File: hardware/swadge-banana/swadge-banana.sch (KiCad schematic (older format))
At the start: 46 parts, among them J1 USB_B_Micro, SW1 SW_SPDT, U1 ESP-13-WROOM-02D, U2 OLED_DISPLAY, U3 BUS_PCIexpress, U4 QMA6981, U5 AP1117-33, U6 OLED_CONNECTOR

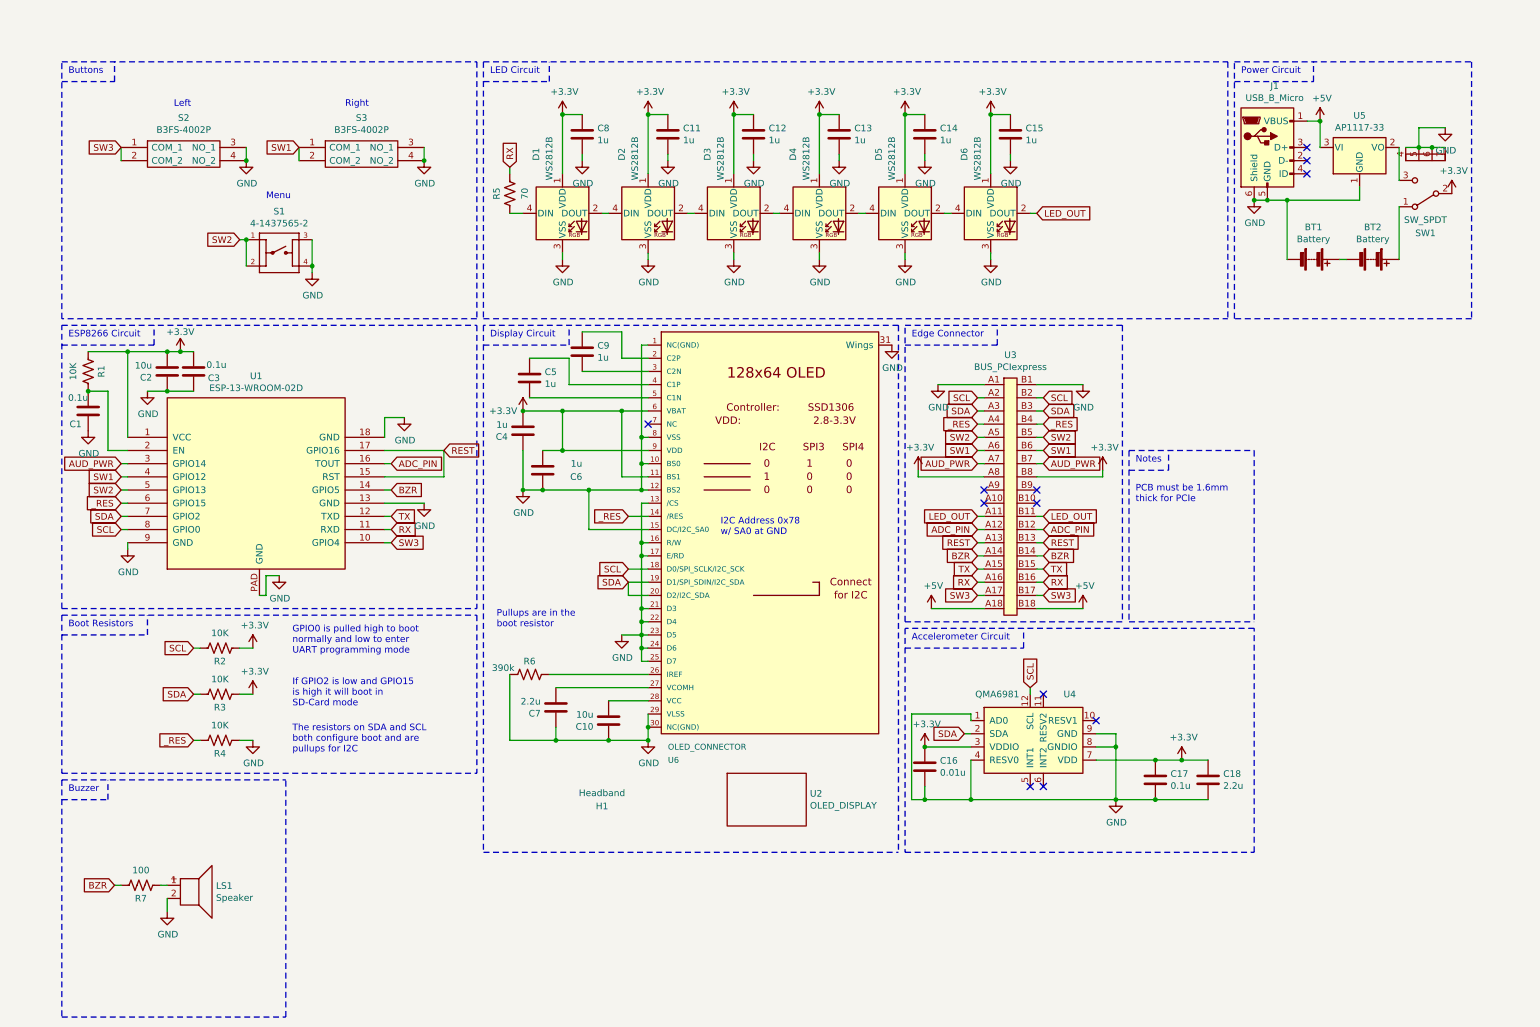
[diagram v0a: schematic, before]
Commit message: Updated banana sch/pcb from barrel
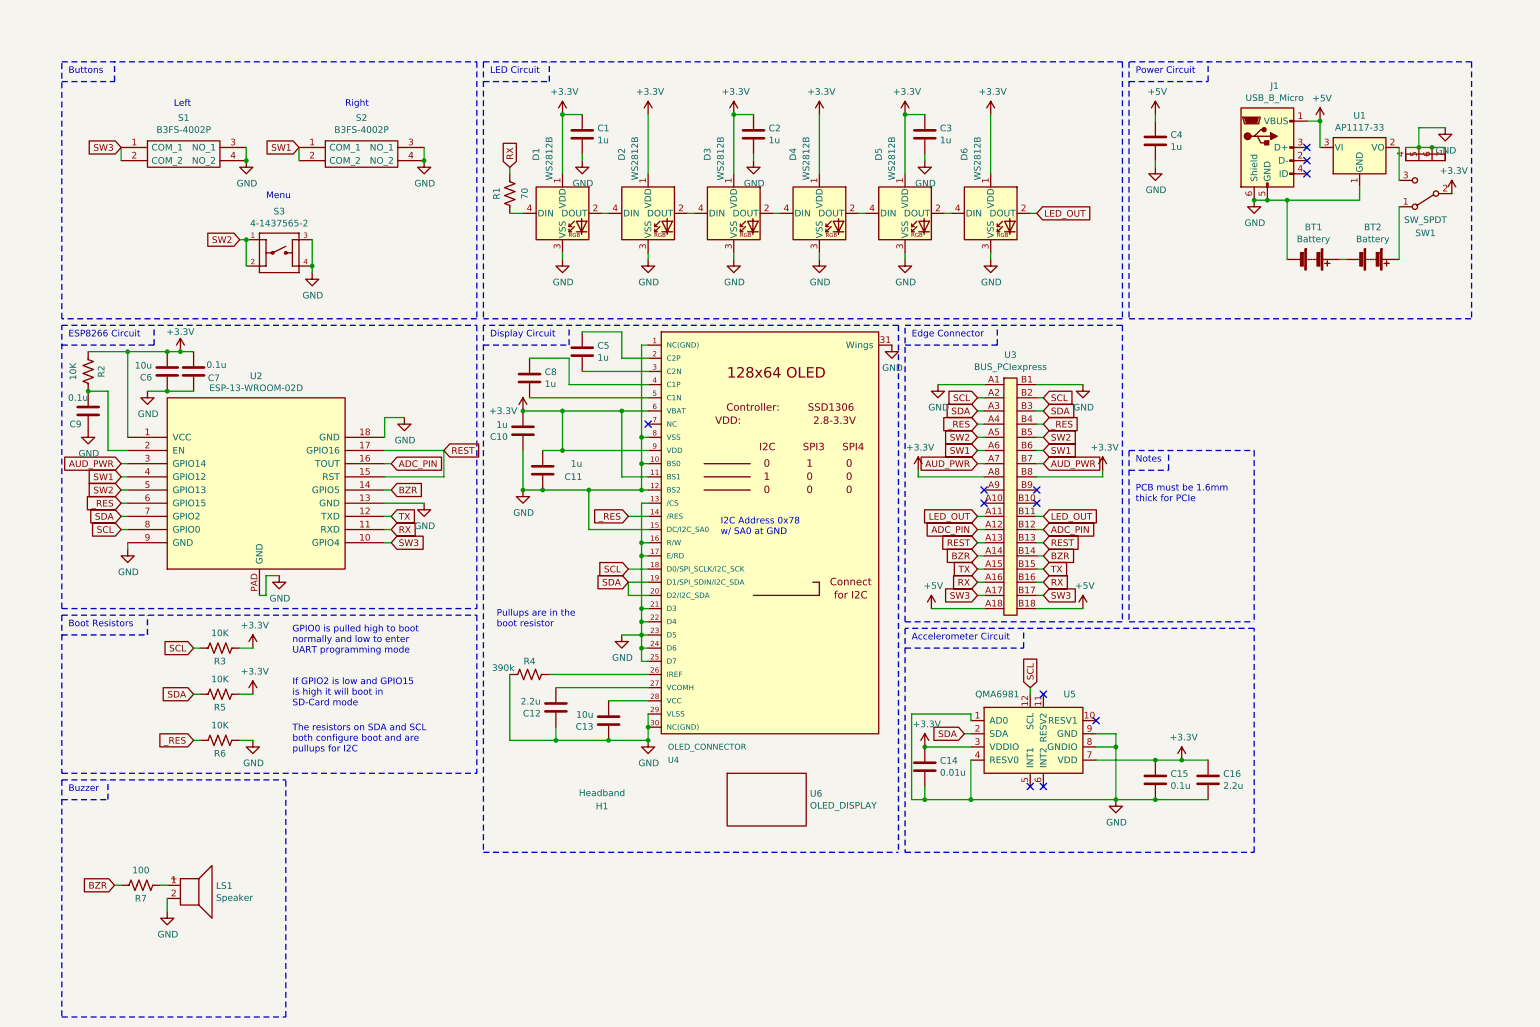
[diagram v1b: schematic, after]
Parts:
- removed C13, C15: 1u, Swadge_Parts:C_0603_1608Metric, symbol Swadge_Parts:C
- U4: renamed from U6; Digikey LCSC #C11095 -> LCSC Part #C11060; Notes Must have top contacts. same as the OLED -> Must have bottom contacts. same as the OLED
- U6: renamed from U2; Digikey EastRising# ER-OLED0.96-1.3W -> EastRising# ER-OLED0.96-1.1W; Notes Must be a single color. white. Must have SSD1306 driver. Mu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 -> Must be a single color; white. Must have SSD1306 driver. Mu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
- renumbered C8 to C1, C4 to C10, C6 to C11, C7 to C12, C10 to C13, C16 to C14, C17 to C15, C18 to C16, C12 to C2, C14 to C3, C11 to C4, C9 to C5, C2 to C6, C3 to C7, C5 to C8, C1 to C9, R5 to R1, R1 to R2, R2 to R3, R6 to R4, R3 to R5, R4 to R6, S2 to S1, S3 to S2, S1 to S3, U5 to U1, U1 to U2, U4 to U5
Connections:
- net +3V3: no longer C4.1
- net +5V: now also C4.1
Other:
- moved on the sheet: C4

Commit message: Merged cnlohr's changes
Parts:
- removed C4: 1u, Swadge_Parts:C_0603_1608Metric, symbol Swadge_Parts:C
- U2: renamed from U6; Digikey EastRising# ER-OLED0.96-1.1W -> EastRising# ER-OLED0.96-1.3W; Notes Must be a single color; white. Must have SSD1306 driver. Mu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 -> Must be a single color. white. Must have SSD1306 driver. Mu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
- U6: renamed from U4; Digikey LCSC Part #C11060 -> LCSC #C11095; Notes Must have bottom contacts. same as the OLED -> Must have top contacts. same as the OLED
- renumbered C9 to C1, C13 to C10, C2 to C12, C3 to C14, C14 to C16, C15 to C17, C16 to C18, C6 to C2, C7 to C3, C10 to C4, C8 to C5, C11 to C6, C12 to C7, C1 to C8, C5 to C9, R2 to R1, R3 to R2, R5 to R3, R6 to R4, R1 to R5, R4 to R6, S3 to S1, S1 to S2, S2 to S3, U2 to U1, U5 to U4, U1 to U5
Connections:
- net +3V3: no longer C3.2
- net +5V: now also C3.2
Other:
- moved on the sheet: C3

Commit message: Added power parts to Swadge_Parts library Modified swadge-banana.sch to use new power parts Removed cnlohr specific paths from sym-lib-table
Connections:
- net labels added: +3V3, +5V
- net labels removed: +3.3V-power, +5V-power
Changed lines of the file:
@@
 	1300 2700 1400 2700
 $Comp
-L 5050RGB:GND #PWR0102
+L Swadge_Parts:GND #PWR0102
 U 1 1 5DB48D54
 P 1900 1250
@@
 Connection ~ 1900 1250
 $Comp
-L 5050RGB:GND #PWR0103
+L Swadge_Parts:GND #PWR0103
 U 1 1 5DB4934E
 P 3250 1250
@@
 Connection ~ 3250 1250
 $Comp
-L 5050RGB:GND #PWR0104
+L Swadge_Parts:GND #PWR0104
 U 1 1 5DB4A3EF
 P 2400 2100
@@
 $EndComp
 $Comp
-L 5050RGB:GND #PWR0105
+L Swadge_Parts:GND #PWR0105
 U 1 1 5DB4B924
 P 3100 3200
@@
 $EndComp
 $Comp
-L 5050RGB:GND #PWR0101
+L Swadge_Parts:GND #PWR0101
 U 1 1 5DB4CC48
 P 1150 3000
@@
 $EndComp
 $Comp
-L 5050RGB:GND #PWR0106
+L Swadge_Parts:GND #PWR0106
 U 1 1 5DB4D3B3
 P 700 3300
@@
 $EndComp
 $Comp
-L 5050RGB:GND #PWR0107
+L Swadge_Parts:GND #PWR0107
 U 1 1 5DB4F15F
 P 3250 3850
@@
 $EndComp
 $Comp
-L 5050RGB:GND #PWR0108
+L Swadge_Parts:GND #PWR0108
 U 1 1 5DB4F885
 P 4000 3800
@@
 Connection ~ 4000 3750
 $Comp
-L 5050RGB:GND #PWR0109
+L Swadge_Parts:GND #PWR0109
 U 1 1 5DB6160F
 P 4300 2000
@@
 $EndComp
 $Comp
-L 5050RGB:GND #PWR0110
+L Swadge_Parts:GND #PWR0110
 U 1 1 5DB61E82
 P 4950 2000
@@
 $EndComp
 $Comp
-L 5050RGB:GND #PWR0111
+L Swadge_Parts:GND #PWR0111
 U 1 1 5DB62589
 P 5600 2000
@@
 $EndComp
 $Comp
-L 5050RGB:GND #PWR0112
+L Swadge_Parts:GND #PWR0112
 U 1 1 5DB62C12
 P 6250 2000
@@
 $EndComp
 $Comp
-L 5050RGB:GND #PWR0113
+L Swadge_Parts:GND #PWR0113
 U 1 1 5DB63381
 P 6900 2000
@@
 $EndComp
 $Comp
-L 5050RGB:GND #PWR0114
+L Swadge_Parts:GND #PWR0114
 U 1 1 5DB63AA7
 P 7550 2000
@@
 $EndComp
 $Comp
-L 5050RGB:GND #PWR0115
+L Swadge_Parts:GND #PWR0115
 U 1 1 5DB661F5
 P 4450 1250
@@
 $EndComp
 $Comp
-L 5050RGB:GND #PWR0116
+L Swadge_Parts:GND #PWR0116
 U 1 1 5DB66B7D
 P 5100 1250
@@
 $EndComp
 $Comp
-L 5050RGB:GND #PWR0117
+L Swadge_Parts:GND #PWR0117
 U 1 1 5DB67441
 P 5750 1250
@@
 $EndComp
 $Comp
-L 5050RGB:GND #PWR0118
+L Swadge_Parts:GND #PWR0118
 U 1 1 5DB67B94
 P 6400 1250
@@
 $EndComp
 $Comp
-L 5050RGB:GND #PWR0119
+L Swadge_Parts:GND #PWR0119
 U 1 1 5DB683CC
 P 7050 1250
@@
 $EndComp
 $Comp
-L 5050RGB:GND #PWR0120
+L Swadge_Parts:GND #PWR0120
 U 1 1 5DB68AB5
 P 7700 1250
@@
 $EndComp
 $Comp
-L 5050RGB:GND #PWR0121
+L Swadge_Parts:GND #PWR0121
 U 1 1 5DB69718
 P 9700 1700
@@
 	9700 1550 9800 1550
 $Comp
-L 5050RGB:GND #PWR0122
+L Swadge_Parts:GND #PWR0122
 U 1 1 5DB80881
 P 11000 1000
@@
 $EndComp
 $Comp
-L 5050RGB:GND #PWR0123
+L Swadge_Parts:GND #PWR0123
 U 1 1 5DB82AD5
 P 6800 2650
@@
 $EndComp
 $Comp
-L 5050RGB:GND #PWR0124
+L Swadge_Parts:GND #PWR0124
 U 1 1 5DB82FEA
 P 7900 2950
@@
 $EndComp
 $Comp
-L 5050RGB:GND #PWR0125
+L Swadge_Parts:GND #PWR0125
 U 1 1 5DB953D8
 P 7500 2950
@@
 $EndComp
 $Comp
-L 5050RGB:GND #PWR0126
+L Swadge_Parts:GND #PWR0126
 U 1 1 5DBBDD93
 P 4150 5750
@@
 	4150 5650 3900 5650
 $Comp
-L 5050RGB:GND #PWR0127
+L Swadge_Parts:GND #PWR0127
 U 1 1 5DBCC3B0
 P 7850 6200
@@
 	7850 6100 8500 6100
 $Comp
-L 5050RGB:GND #PWR0128
+L Swadge_Parts:GND #PWR0128
 U 1 1 5DBDEED6
 P 1950 5650
@@
 $EndComp
 $Comp
-L 5050RGB:GND #PWR0129
+L Swadge_Parts:GND #PWR0129
 U 1 1 5DBDF629
 P 2150 4400
@@
 $EndComp
 $Comp
-L 5050RGB:GND #PWR0130
+L Swadge_Parts:GND #PWR0130
 U 1 1 5DBDFF8F
 P 1000 4200
@@
 $EndComp
 $Comp
-L 5050RGB:GND #PWR0131
+L Swadge_Parts:GND #PWR0131
 U 1 1 5DBE4C6E
 P 4750 4850
@@
 $EndComp
 $Comp
-L 5050RGB:GND #PWR0132
+L Swadge_Parts:GND #PWR0132
 U 1 1 5DBE56FB
 P 1300 6950
@@
 $EndComp
 $Comp
-L swadge-banana-rescue:+3.3V-power #PWR0133
+L Swadge_Parts:+3V3 #PWR0133
 U 1 1 5DBEBACC
 P 8400 3600
 F 0 "#PWR0133" H 8400 3450 50  0001 C CNN
-F 1 "+3.3V-power" H 8415 3773 50  0000 C CNN
+F 1 "+3V3" H 8415 3773 50  0000 C CNN
 F 2 "" H 8400 3600 50  0001 C CNN
 F 3 "" H 8400 3600 50  0001 C CNN
@@
 $EndComp
 $Comp
-L swadge-banana-rescue:+3.3V-power #PWR0134
+L Swadge_Parts:+3V3 #PWR0134
 U 1 1 5DBF32F8
 P 7000 3600
 F 0 "#PWR0134" H 7000 3450 50  0001 C CNN
-F 1 "+3.3V-power" H 7015 3773 50  0000 C CNN
+F 1 "+3V3" H 7015 3773 50  0000 C CNN
 F 2 "" H 7000 3600 50  0001 C CNN
 F 3 "" H 7000 3600 50  0001 C CNN
@@
 $EndComp
 $Comp
-L swadge-banana-rescue:+3.3V-power #PWR0135
+L Swadge_Parts:+3V3 #PWR0135
 U 1 1 5DBF407A
 P 3900 3150
 F 0 "#PWR0135" H 3900 3000 50  0001 C CNN
-F 1 "+3.3V-power" H 3915 3323 50  0000 C CNN
+F 1 "+3V3" H 3915 3323 50  0000 C CNN
 F 2 "" H 3900 3150 50  0001 C CNN
 F 3 "" H 3900 3150 50  0001 C CNN
@@
 Connection ~ 4000 3150
 $Comp
-L swadge-banana-rescue:+3.3V-power #PWR0136
+L Swadge_Parts:+3V3 #PWR0136
 U 1 1 5DC043FE
 P 7650 900
 F 0 "#PWR0136" H 7650 750 50  0001 C CNN
-F 1 "+3.3V-power" H 7665 1073 50  0000 C CNN
+F 1 "+3V3" H 7665 1073 50  0000 C CNN
 F 2 "" H 7650 900 50  0001 C CNN
 F 3 "" H 7650 900 50  0001 C CNN
@@
 	7650 900  7550 900
 $Comp
-L swadge-banana-rescue:+3.3V-power #PWR0137
+L Swadge_Parts:+3V3 #PWR0137
 U 1 1 5DC21159
 P 7000 900
 F 0 "#PWR0137" H 7000 750 50  0001 C CNN
-F 1 "+3.3V-power" H 7015 1073 50  0000 C CNN
+F 1 "+3V3" H 7015 1073 50  0000 C CNN
 F 2 "" H 7000 900 50  0001 C CNN
 F 3 "" H 7000 900 50  0001 C CNN
@@
 	7000 900  6900 900
 $Comp
-L swadge-banana-rescue:+3.3V-power #PWR0138
+L Swadge_Parts:+3V3 #PWR0138
 U 1 1 5DC21711
 P 6350 900
 F 0 "#PWR0138" H 6350 750 50  0001 C CNN
-F 1 "+3.3V-power" H 6365 1073 50  0000 C CNN
+F 1 "+3V3" H 6365 1073 50  0000 C CNN
 F 2 "" H 6350 900 50  0001 C CNN
 F 3 "" H 6350 900 50  0001 C CNN
@@
 	6350 900  6250 900
 $Comp
-L swadge-banana-rescue:+3.3V-power #PWR0139
+L Swadge_Parts:+3V3 #PWR0139
 U 1 1 5DC21C53
 P 5700 900
 F 0 "#PWR0139" H 5700 750 50  0001 C CNN
-F 1 "+3.3V-power" H 5715 1073 50  0000 C CNN
+F 1 "+3V3" H 5715 1073 50  0000 C CNN
 F 2 "" H 5700 900 50  0001 C CNN
 F 3 "" H 5700 900 50  0001 C CNN
@@
 	5700 900  5750 900
 $Comp
-L swadge-banana-rescue:+3.3V-power #PWR0140
+L Swadge_Parts:+3V3 #PWR0140
 U 1 1 5DC2220F
 P 5050 900
 F 0 "#PWR0140" H 5050 750 50  0001 C CNN
-F 1 "+3.3V-power" H 5065 1073 50  0000 C CNN
+F 1 "+3V3" H 5065 1073 50  0000 C CNN
 F 2 "" H 5050 900 50  0001 C CNN
 F 3 "" H 5050 900 50  0001 C CNN
@@
 	5050 900  4950 900
 $Comp
-L swadge-banana-rescue:+3.3V-power #PWR0141
+L Swadge_Parts:+3V3 #PWR0141
 U 1 1 5DC2439B
 P 4400 900
 F 0 "#PWR0141" H 4400 750 50  0001 C CNN
-F 1 "+3.3V-power" H 4415 1073 50  0000 C CNN
+F 1 "+3V3" H 4415 1073 50  0000 C CNN
 F 2 "" H 4400 900 50  0001 C CNN
 F 3 "" H 4400 900 50  0001 C CNN
@@
 	4400 900  4300 900
 $Comp
-L swadge-banana-rescue:+3.3V-power #PWR0142
+L Swadge_Parts:+3V3 #PWR0142
 U 1 1 5DC2A665
 P 1400 2700
 F 0 "#PWR0142" H 1400 2550 50  0001 C CNN
-F 1 "+3.3V-power" H 1415 2873 50  0000 C CNN
+F 1 "+3V3" H 1415 2873 50  0000 C CNN
 F 2 "" H 1400 2700 50  0001 C CNN
 F 3 "" H 1400 2700 50  0001 C CNN
@@
 $EndComp
 $Comp
-L swadge-banana-rescue:+3.3V-power #PWR0143
+L Swadge_Parts:+3V3 #PWR0143
 U 1 1 5DC32845
 P 1950 4950
 F 0 "#PWR0143" H 1950 4800 50  0001 C CNN
-F 1 "+3.3V-power" H 1965 5123 50  0000 C CNN
+F 1 "+3V3" H 1965 5123 50  0000 C CNN
 F 2 "" H 1950 4950 50  0001 C CNN
 F 3 "" H 1950 4950 50  0001 C CNN
@@
 $EndComp
 $Comp
-L swadge-banana-rescue:+3.3V-power #PWR0144
+L Swadge_Parts:+3V3 #PWR0144
 U 1 1 5DC361A8
 P 1950 5300
 F 0 "#PWR0144" H 1950 5150 50  0001 C CNN
-F 1 "+3.3V-power" H 1965 5473 50  0000 C CNN
+F 1 "+3V3" H 1965 5473 50  0000 C CNN
 F 2 "" H 1950 5300 50  0001 C CNN
 F 3 "" H 1950 5300 50  0001 C CNN
@@
 $EndComp
 $Comp
-L swadge-banana-rescue:+3.3V-power #PWR0145
+L Swadge_Parts:+3V3 #PWR0145
 U 1 1 5DC3D4B5
 P 9050 5800
 F 0 "#PWR0145" H 9050 5650 50  0001 C CNN
-F 1 "+3.3V-power" H 9065 5973 50  0000 C CNN
+F 1 "+3V3" H 9065 5973 50  0000 C CNN
 F 2 "" H 9050 5800 50  0001 C CNN
 F 3 "" H 9050 5800 50  0001 C CNN
@@
 	9050 5800 9200 5800
 $Comp
-L swadge-banana-rescue:+3.3V-power #PWR0146
+L Swadge_Parts:+3V3 #PWR0146
 U 1 1 5DC3EBBA
 P 7100 5700
 F 0 "#PWR0146" H 7100 5550 50  0001 C CNN
-F 1 "+3.3V-power" H 7115 5873 50  0000 C CNN
+F 1 "+3V3" H 7115 5873 50  0000 C CNN
 F 2 "" H 7100 5700 50  0001 C CNN
 F 3 "" H 7100 5700 50  0001 C CNN
@@
 	7100 5700 7400 5700
 $Comp
-L swadge-banana-rescue:+3.3V-power #PWR0147
+L Swadge_Parts:+3V3 #PWR0147
 U 1 1 5DC46776
 P 11050 1500
 F 0 "#PWR0147" H 11050 1350 50  0001 C CNN
-F 1 "+3.3V-power" H 11065 1673 50  0000 C CNN
+F 1 "+3V3" H 11065 1673 50  0000 C CNN
 F 2 "" H 11050 1500 50  0001 C CNN
 F 3 "" H 11050 1500 50  0001 C CNN
@@
 $EndComp
 $Comp
-L swadge-banana-rescue:+5V-power #PWR0148
+L Swadge_Parts:+5V #PWR0148
 U 1 1 5DC4F279
 P 10050 950
 F 0 "#PWR0148" H 10050 800 50  0001 C CNN
-F 1 "+5V-power" H 10065 1123 50  0000 C CNN
+F 1 "+5V" H 10065 1123 50  0000 C CNN
 F 2 "" H 10050 950 50  0001 C CNN
 F 3 "" H 10050 950 50  0001 C CNN
@@
 Connection ~ 10050 950
 $Comp
-L swadge-banana-rescue:+5V-power #PWR0149
+L Swadge_Parts:+5V #PWR0149
 U 1 1 5DC5326C
 P 8250 4650
 F 0 "#PWR0149" H 8250 4500 50  0001 C CNN
-F 1 "+5V-power" H 8265 4823 50  0000 C CNN
+F 1 "+5V" H 8265 4823 50  0000 C CNN
 F 2 "" H 8250 4650 50  0001 C CNN
 F 3 "" H 8250 4650 50  0001 C CNN
@@
 $EndComp
 $Comp
-L swadge-banana-rescue:+5V-power #PWR0150
+L Swadge_Parts:+5V #PWR0150
 U 1 1 5DC5B61A
 P 7100 4650
 F 0 "#PWR0150" H 7100 4500 50  0001 C CNN
-F 1 "+5V-power" H 7115 4823 50  0000 C CNN
+F 1 "+5V" H 7115 4823 50  0000 C CNN
 F 2 "" H 7100 4650 50  0001 C CNN
 F 3 "" H 7100 4650 50  0001 C CNN
@@
 $EndComp
 $Comp
-L 5050RGB:GND #PWR?
+L Swadge_Parts:GND #PWR?
 U 1 1 5DCB537C
 P 10750 1000
@@
 $EndComp
 $Comp
-L swadge-banana-rescue:+5V-power #PWR?
+L Swadge_Parts:+5V #PWR?
 U 1 1 5DCB567C
 P 10750 700
 F 0 "#PWR?" H 10750 550 50  0001 C CNN
-F 1 "+5V-power" H 10765 873 50  0000 C CNN
+F 1 "+5V" H 10765 873 50  0000 C CNN
 F 2 "" H 10750 700 50  0001 C CNN
 F 3 "" H 10750 700 50  0001 C CNN

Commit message: Copied schematic from barrel, again Reimported schematic into layout, fixed capacitor changes Fixed one DRC violation
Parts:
- added C4: 1u, Swadge_Parts:C_0603_1608Metric, symbol Swadge_Parts:C
- added H2: Headband, Swadge_Parts:NULL, symbol Swadge_Parts:Headband
- U4: renamed from U6; Digikey LCSC #C11095 -> LCSC Part #C11060; Notes Must have top contacts. same as the OLED -> Must have bottom contacts. same as the OLED
- U6: renamed from U2; Digikey EastRising# ER-OLED0.96-1.3W -> EastRising# ER-OLED0.96-1.1W; Notes Must be a single color. white. Must have SSD1306 driver. Mu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 -> Must be a single color; white. Must have SSD1306 driver. Mu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
- renumbered C8 to C1, C4 to C10, C6 to C11, C7 to C12, C10 to C13, C16 to C14, C17 to C15, C18 to C16, C12 to C2, C14 to C3, C9 to C5, C2 to C6, C3 to C7, C5 to C8, C1 to C9, R5 to R1, R1 to R2, R2 to R3, R6 to R4, R3 to R5, R4 to R6, S2 to S1, S3 to S2, S1 to S3, U5 to U1, U1 to U2, U4 to U5
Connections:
- wire segments 220 -> 205
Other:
- moved on the sheet: C7

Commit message: (Banana this time) Changed I2C pullups to 1K Updated digikey part numbers on BOM
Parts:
- C14: Digikey 1276-1000-1-ND -> 1292-1622-2-ND
- R3, R5: value 10K -> 1K; Digikey RNCP0603FTD10K0CT-ND -> 2037-PFR05S-102-FNHTR-ND
- R7: Digikey RNCP0603FTD10K0CT-ND -> 311-100JRTR-ND
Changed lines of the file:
@@
 P 1700 4950
 F 0 "R3" V 1800 4950 50  0000 C CNN
-F 1 "10K" V 1586 4950 50  0000 C CNN
+F 1 "1K" V 1586 4950 50  0000 C CNN
 F 2 "Swadge_Parts:R_0603_1608Metric" V 1740 4940 50  0001 C CNN
 F 3 "" H 1700 4950 50  0001 C CNN
 F 4 "10" H 0   0   50  0001 C CNN "Cost100"
-F 5 "RNCP0603FTD10K0CT-ND" H 0   0   50  0001 C CNN "Digikey"
+F 5 "2037-PFR05S-102-FNHTR-ND" H 0   0   50  0001 C CNN "Digikey"
 F 6 "Y" H 0   0   50  0001 C CNN "Substitutable"
 F 7 "0603 Package" H 1700 4950 50  0001 C CNN "Notes"
@@
 P 1700 5300
 F 0 "R5" V 1800 5300 50  0000 C CNN
-F 1 "10K" V 1586 5300 50  0000 C CNN
+F 1 "1K" V 1586 5300 50  0000 C CNN
 F 2 "Swadge_Parts:R_0603_1608Metric" V 1740 5290 50  0001 C CNN
 F 3 "" H 1700 5300 50  0001 C CNN
 F 4 "10" H 0   0   50  0001 C CNN "Cost100"
-F 5 "RNCP0603FTD10K0CT-ND" H 0   0   50  0001 C CNN "Digikey"
+F 5 "2037-PFR05S-102-FNHTR-ND" H 0   0   50  0001 C CNN "Digikey"
 F 6 "Y" H 0   0   50  0001 C CNN "Substitutable"
 F 7 "0603 Package" H 1700 5300 50  0001 C CNN "Notes"
@@
 F 3 "" H 7050 5850 50  0001 C CNN
 F 4 "10" H 4200 -1100 50  0001 C CNN "Cost100"
-F 5 "1276-1000-1-ND" H 4200 -1100 50  0001 C CNN "Digikey"
+F 5 "1292-1622-2-ND" H 4200 -1100 50  0001 C CNN "Digikey"
 F 6 "Y" H 4200 -1100 50  0001 C CNN "Substitutable"
 F 7 "0603 Package" H 7050 5850 50  0001 C CNN "Notes"
@@
 F 3 "" H 1100 6750 50  0001 C CNN
 F 4 "10" H -600 1100 50  0001 C CNN "Cost100"
-F 5 "RNCP0603FTD10K0CT-ND" H -600 1100 50  0001 C CNN "Digikey"
+F 5 "311-100JRTR-ND" H -600 1100 50  0001 C CNN "Digikey"
 F 6 "Y" H -600 1100 50  0001 C CNN "Substitutable"
 F 7 "0603 Package" H 1100 6750 50  0001 C CNN "Notes"

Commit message: Added series I2C resistors to QMA6981 (Banana)
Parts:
- added R8, R9: 47, Swadge_Parts:R_0603_1608Metric, symbol Swadge_Parts:R_US
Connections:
- wire segments 205 -> 208
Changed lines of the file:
@@
 	1    0    0    -1
 $EndComp
-Text GLabel 7350 5600 0    50   Input ~ 0
+Text GLabel 7050 5250 1    50   Input ~ 0
 SDA
-Text GLabel 7850 5250 1    50   Input ~ 0
+Text GLabel 8200 5100 2    50   Input ~ 0
 SCL
 NoConn ~ 7850 6000
@@
 	8800 6100 8500 6100
 Connection ~ 8800 6100
-Wire Wire Line
-	7850 5250 7850 5300
 Wire Wire Line
 	7350 5600 7400 5600
@@
 	1    0    0    -1
 $EndComp
+$Comp
+L Swadge_Parts:R_US R9
+U 1 1 5DCFA389
+P 8000 5100
+F 0 "R9" V 8100 5100 50  0000 C CNN
+F 1 "47" V 7886 5100 50  0000 C CNN
+F 2 "Swadge_Parts:R_0603_1608Metric" V 8040 5090 50  0001 C CNN
+F 3 "" H 8000 5100 50  0001 C CNN
+F 4 "10" H 6300 150 50  0001 C CNN "Cost100"
+F 5 "RMCF0603FT47R0TR-ND" H 6300 150 50  0001 C CNN "Digikey"
+F 6 "Y" H 6300 150 50  0001 C CNN "Substitutable"
+F 7 "0603 Package" H 8000 5100 50  0001 C CNN "Notes"
+	1    8000 5100
+	0    1    1    0
+$EndComp
+Wire Wire Line
+	8200 5100 8150 5100
+Wire Wire Line
+	7850 5100 7850 5300
+Wire Wire Line
+	7050 5250 7050 5300
+Wire Wire Line
+	7350 5300 7350 5600
+$Comp
+L Swadge_Parts:R_US R8
+U 1 1 5DD38085
+P 7200 5300
+F 0 "R8" V 7300 5300 50  0000 C CNN
+F 1 "47" V 7086 5300 50  0000 C CNN
+F 2 "Swadge_Parts:R_0603_1608Metric" V 7240 5290 50  0001 C CNN
+F 3 "" H 7200 5300 50  0001 C CNN
+F 4 "10" H 5500 350 50  0001 C CNN "Cost100"
+F 5 "RMCF0603FT47R0TR-ND" H 5500 350 50  0001 C CNN "Digikey"
+F 6 "Y" H 5500 350 50  0001 C CNN "Substitutable"
+F 7 "0603 Package" H 7200 5300 50  0001 C CNN "Notes"
+	1    7200 5300
+	0    1    1    0
+$EndComp
 $EndSCHEMATC

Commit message: Added new QMA6981 part with larger pads Updated banana and barrel with new pads
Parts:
- U5: footprint Swadge_Parts:QMA6981 -> Swadge_Parts:QMA6981_2
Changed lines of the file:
@@
 F 0 "U5" H 8150 6000 50  0000 C CNN
 F 1 "QMA6981" H 7600 6000 50  0000 C CNN
-F 2 "Swadge_Parts:QMA6981" H 7700 6350 50  0001 C CNN
+F 2 "Swadge_Parts:QMA6981_2" H 7700 6350 50  0001 C CNN
 F 3 "https://datasheet.lcsc.com/szlcsc/QST-QMA6981_C310611.pdf" H 7900 5600 50  0001 C CNN
 F 4 "LCSC Part #C310611" H 7600 6450 50  0001 C CNN "Digikey"
